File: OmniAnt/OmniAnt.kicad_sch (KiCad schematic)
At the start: 19 parts, among them J1 Conn_01x02_Pin, J3 Connector, USB-TYPE-C-16P, U1 ESP32-S3-WROOM-1, U2 TPSM53603RDA, U4 USBLC6-2P6

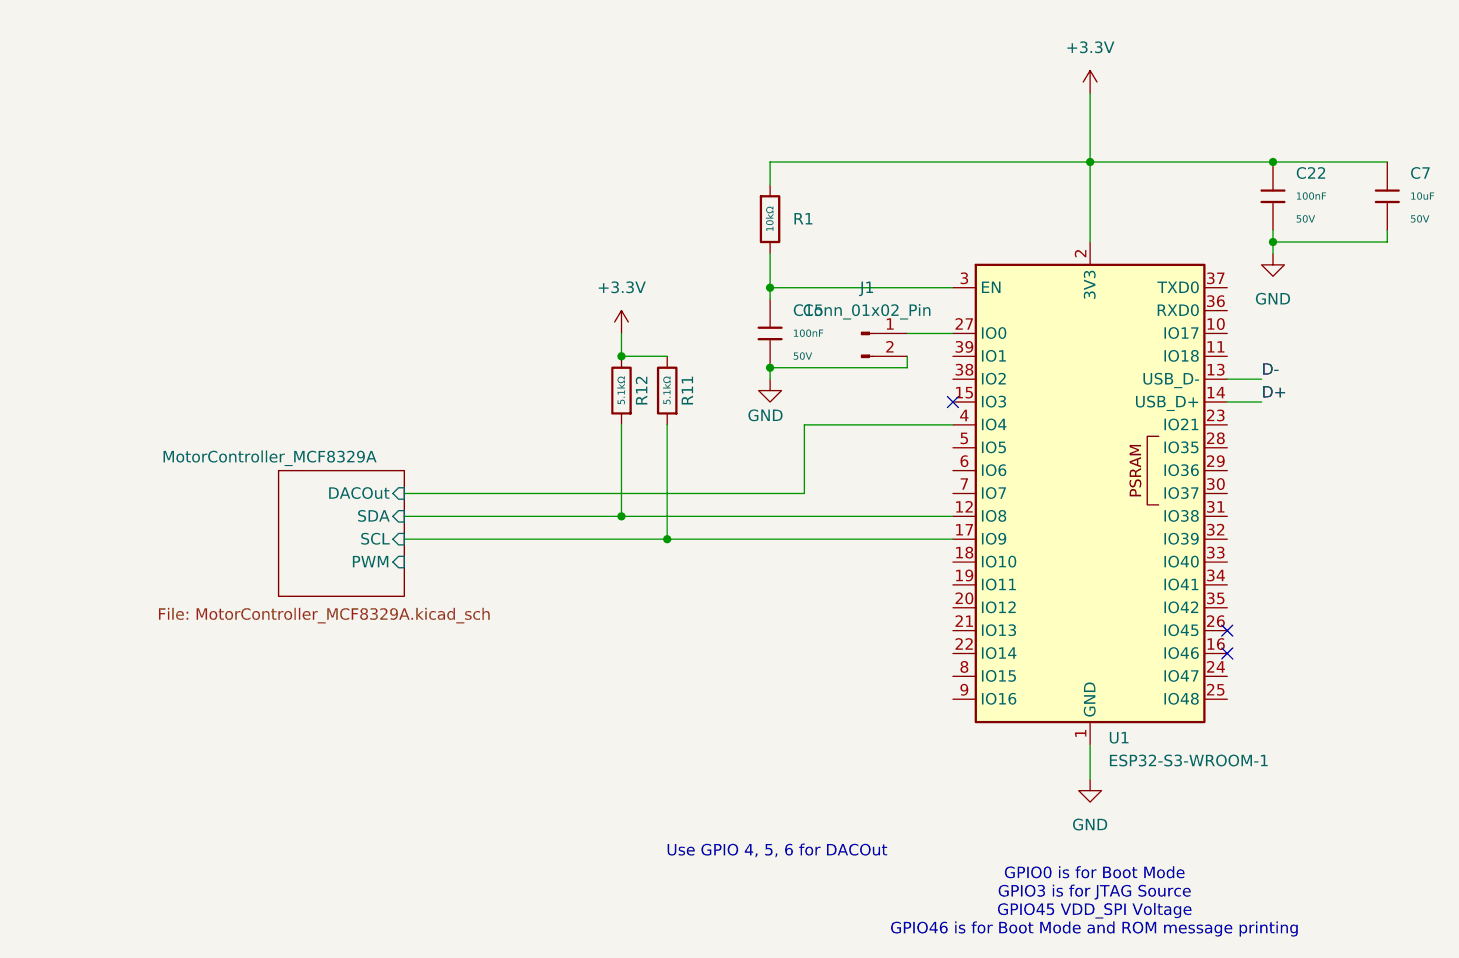
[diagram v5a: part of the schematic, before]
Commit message: I added a green LED.
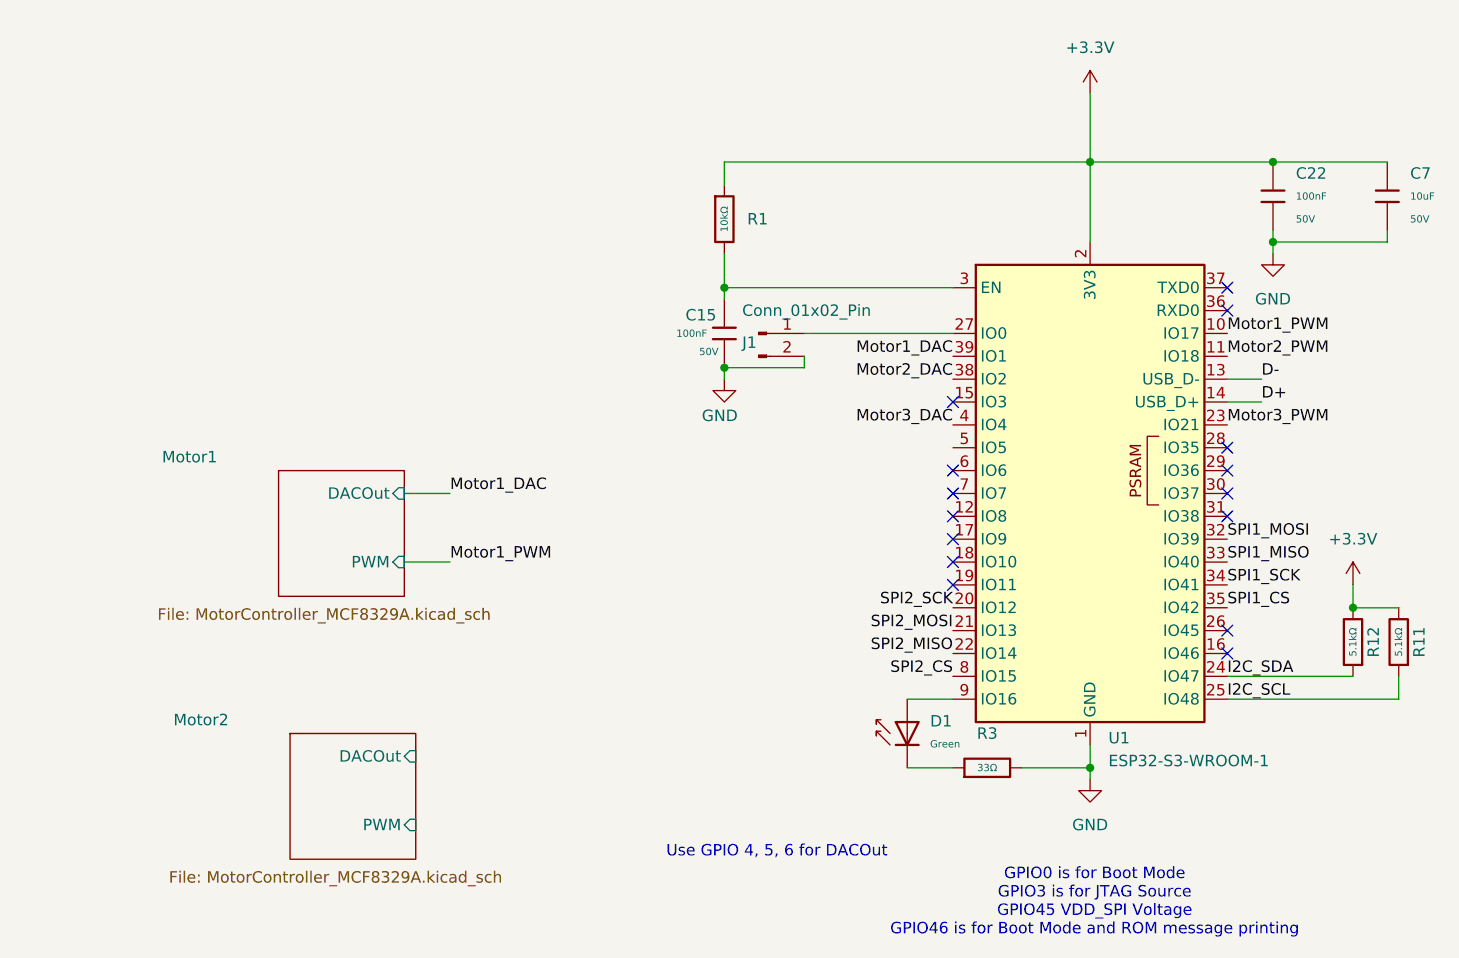
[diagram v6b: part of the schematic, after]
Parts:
- added D1: Green, PCM_JLCPCB:D_0805, symbol PCM_JLCPCB-Diodes:LED,0805,Green
- added R3: 33Ω, PCM_JLCPCB:R_0402, symbol PCM_JLCPCB-Resistors:0402,33Ω
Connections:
- net GND: now also R3.2
- net Motor1_PWM: now reaches U1.10 (IO17)
- net Motor2_PWM: now reaches U1.11 (IO18)
- net SPI2_SCK: now reaches U1.20 (IO12)
- net SPI2_MOSI: now reaches U1.21 (IO13)
- net SPI2_MISO: now reaches U1.22 (IO14)
- net Motor3_PWM: now reaches U1.23 (IO21)
- net I2C_SDA: now reaches U1.24 (IO47)
- net I2C_SDA: now also R12.1
- net I2C_SCL: now reaches U1.25 (IO48)
- net I2C_SCL: now also R11.1
- net SPI1_MOSI: now reaches U1.32 (IO39)
- net SPI1_MISO: now reaches U1.33 (IO40)
- net SPI1_SCK: now reaches U1.34 (IO41)
- net SPI1_CS: now reaches U1.35 (IO42)
- net Motor2_DAC: now reaches U1.38 (IO2)
- net Motor1_DAC: now reaches U1.39 (IO1)
- net SPI2_CS: now reaches U1.8 (IO15)
- net at U1.9 (IO16): now also D1.2
- net Motor1/DACOut renamed Motor3_DAC
- net Motor1/SCL: no longer names the net of U1.17 (IO9)
- net Motor1/SCL: no longer R11.1
- net Motor1/SDA: no longer names the net of U1.12 (IO8)
- net Motor1/SDA: no longer R12.1
- new net: D1.1, R3.1
- no-connect marks 7 -> 19
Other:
- sheet MotorController_MCF8329A renamed Motor1
- added sheet Motor2 (MotorController_MCF8329A.kicad_sch)
- sheet Motor1 ports: added none; removed SCL, SDA
- moved on the sheet: C15, J1, R1, R11, R12

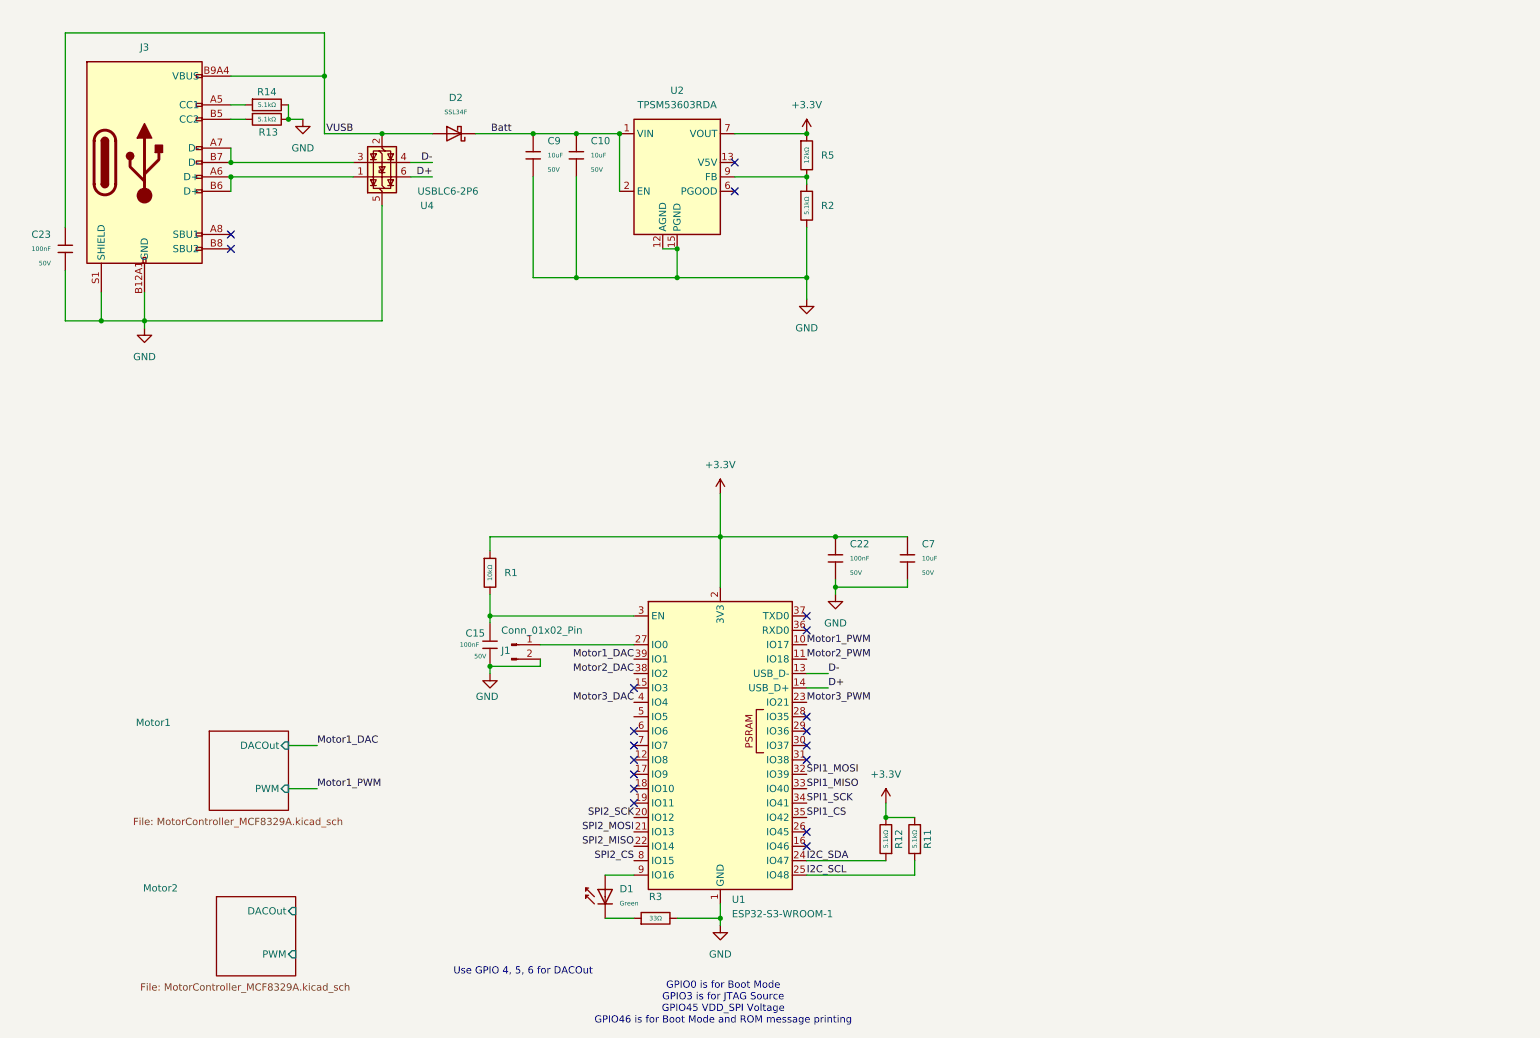
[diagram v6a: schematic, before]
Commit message: I added in addressable LEDs, the accelerometers, and some inputs from a receiver just in case.
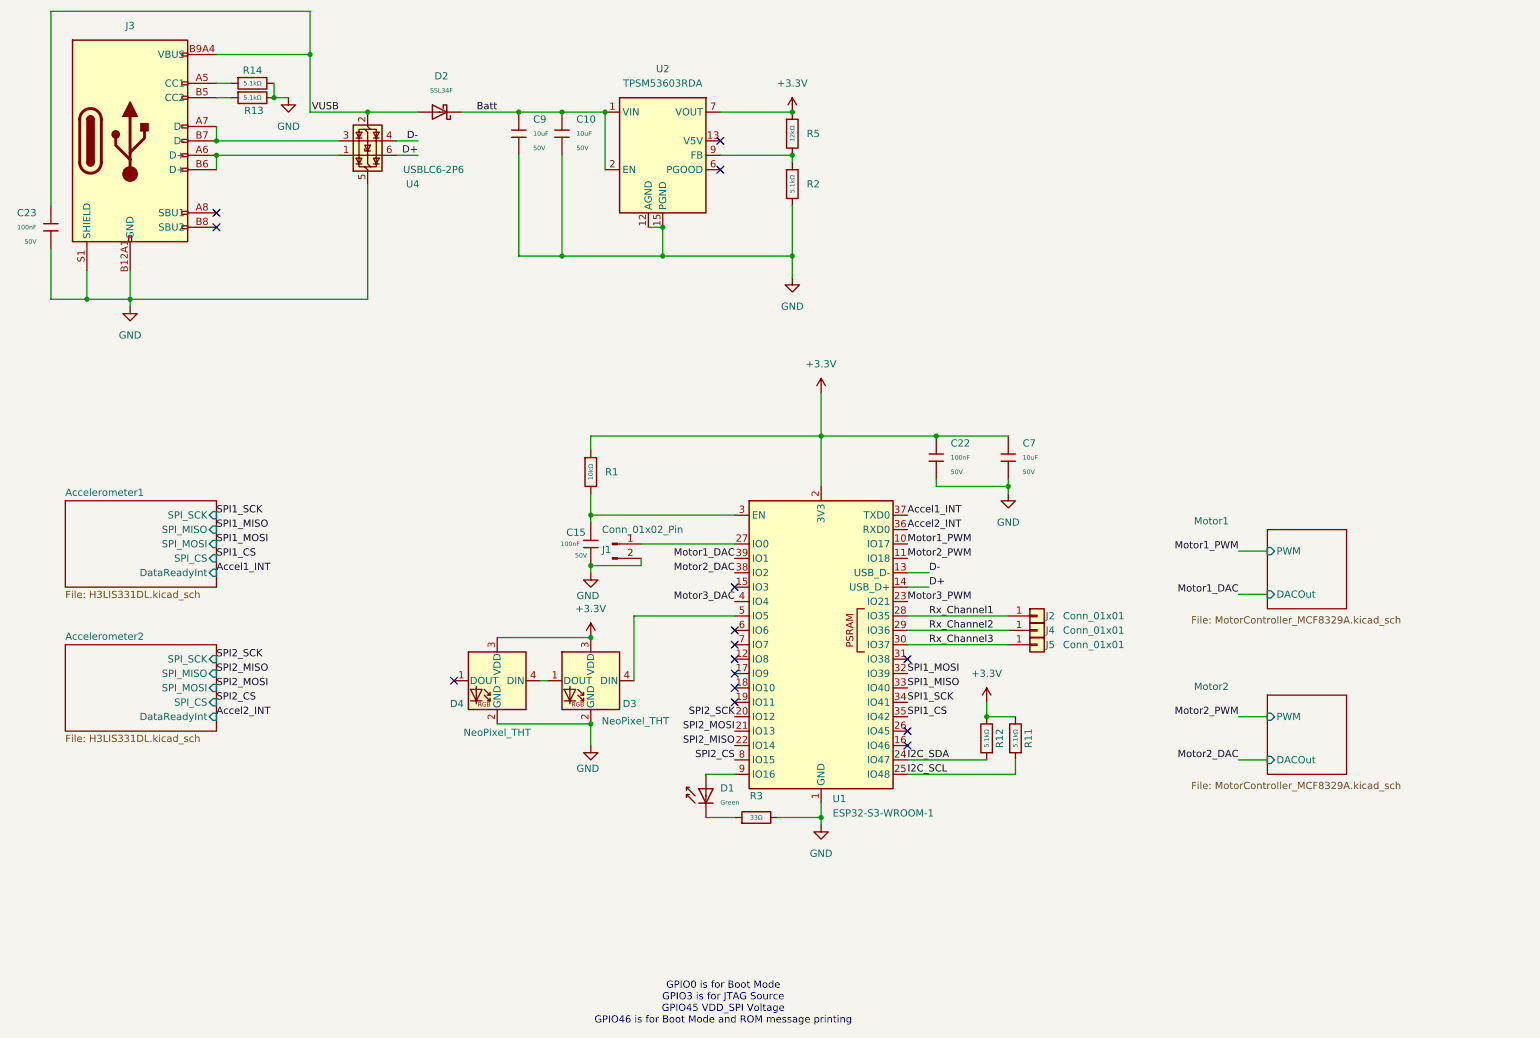
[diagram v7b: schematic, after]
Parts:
- added D3, D4: NeoPixel_THT, LED_THT:LED_D5.0mm-4_RGB, symbol LED:NeoPixel_THT
- added J2, J4, J5: Conn_01x01, symbol Connector_Generic:Conn_01x01
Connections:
- net +3.3V: now also D3.3 (VDD), D4.3 (VDD)
- net GND: now also D3.2 (GND), D4.2 (GND)
- net Rx_Channel1: now reaches U1.28 (IO35)
- net Rx_Channel1: now also J2.1 (Pin_1)
- net Rx_Channel2: now reaches U1.29 (IO36)
- net Rx_Channel2: now also J4.1 (Pin_1)
- net Rx_Channel3: now reaches U1.30 (IO37)
- net Rx_Channel3: now also J5.1 (Pin_1)
- net Accel2_INT: now reaches U1.36 (RXD0)
- net Accel1_INT: now reaches U1.37 (TXD0)
- net at U1.5 (IO5): now also D3.4 (DIN)
- new net: D3.1 (DOUT), D4.4 (DIN)
- no-connect marks 19 -> 15
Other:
- added sheet Accelerometer1 (H3LIS331DL.kicad_sch)
- added sheet Accelerometer2 (H3LIS331DL.kicad_sch)
- note removed: "Use GPIO 4, 5, 6 for DACOut"
- moved on the sheet: C10, C15, C22, C23, C7, C9, D1, D2, J1, J3, R1, R11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

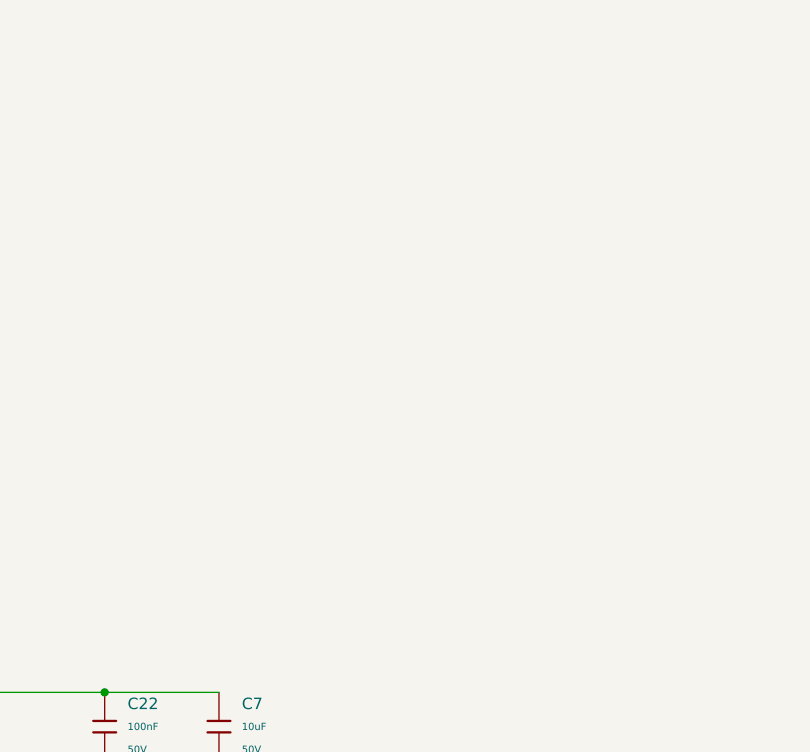
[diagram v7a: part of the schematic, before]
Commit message: I added in the XT30 Connectors for the batteries
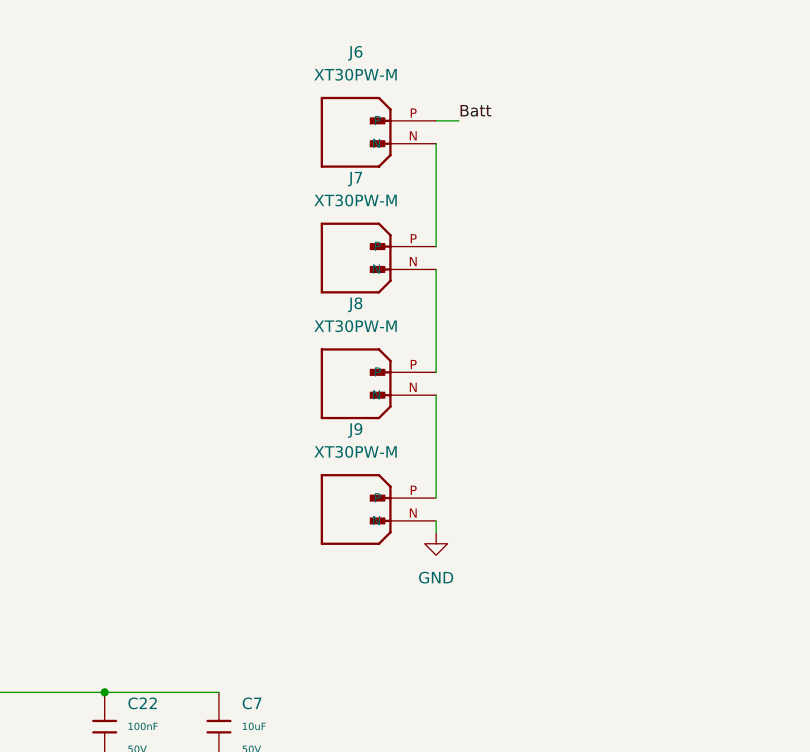
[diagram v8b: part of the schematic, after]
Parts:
- added J6, J7, J8, J9: XT30PW-M, Footprints:AMASS_XT30PW-M, symbol XT30PW-M:XT30PW-M
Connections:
- net Batt: now also J6.P
- net GND: now also J9.N
- new net: J8.N, J9.P
- new net: J6.N, J7.P
- new net: J7.N, J8.P
